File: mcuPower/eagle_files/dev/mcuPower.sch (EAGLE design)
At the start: 8 parts, among them P1 CR2032, P2 CR2032, U1 PQ070XF01SZH

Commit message: various changes + production files. Reroutes, library footprint changes, and moving pot to front side of board
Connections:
- net VOUT: now also R2.E; no longer R2.A
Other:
- moved on the sheet: R2
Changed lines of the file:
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@@
 <instance part="C1" gate="G$1" x="33.02" y="53.34"/>
 <instance part="C2" gate="G$1" x="55.88" y="50.8"/>
-<instance part="R2" gate="1" x="76.2" y="50.8" rot="R180"/>
+<instance part="R2" gate="1" x="76.2" y="50.8"/>
 <instance part="SUPPLY1" gate="G$1" x="53.34" y="96.52"/>
 <instance part="SUPPLY2" gate="GND" x="-10.16" y="27.94"/>
@@
 <wire x1="86.36" y1="58.42" x2="83.82" y2="58.42" width="0.1524" layer="91"/>
 <wire x1="83.82" y1="58.42" x2="83.82" y2="63.5" width="0.1524" layer="91"/>
-<junction x="81.28" y="43.18"/>
-<wire x1="81.28" y1="43.18" x2="68.58" y2="43.18" width="0.1524" layer="91"/>
-<wire x1="68.58" y1="43.18" x2="68.58" y2="50.8" width="0.1524" layer="91"/>
+<pinref part="U1" gate="G$1" pin="VADJ"/>
 <pinref part="R2" gate="1" pin="S"/>
-<wire x1="68.58" y1="50.8" x2="71.12" y2="50.8" width="0.1524" layer="91"/>
-<pinref part="U1" gate="G$1" pin="VADJ"/>
+<wire x1="81.28" y1="48.26" x2="81.28" y2="50.8" width="0.1524" layer="91"/>
+<junction x="81.28" y="48.26"/>
 </segment>
 </net>
@@
 <wire x1="55.88" y1="58.42" x2="55.88" y2="53.34" width="0.1524" layer="91"/>
 <label x="68.58" y="58.42" size="1.778" layer="95"/>
+<pinref part="U1" gate="G$1" pin="VOUT"/>
+<pinref part="R2" gate="1" pin="E"/>
+<wire x1="76.2" y1="55.88" x2="76.2" y2="58.42" width="0.1524" layer="91"/>
 <junction x="76.2" y="58.42"/>
-<pinref part="R2" gate="1" pin="A"/>
-<wire x1="76.2" y1="58.42" x2="76.2" y2="55.88" width="0.1524" layer="91"/>
-<pinref part="U1" gate="G$1" pin="VOUT"/>
 </segment>
 <segment>

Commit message: added extra header pin to stabilize board
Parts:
- added JP2: (no value), adafruit:PINHD-1X1
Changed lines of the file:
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@@
 <part name="P1" library="freddyLibr" deviceset="CR2032" device=""/>
 <part name="P2" library="freddyLibr" deviceset="CR2032" device=""/>
+<part name="JP2" library="adafruit" deviceset="PINHD-1X1" device=""/>
 </parts>
 <sheets>
@@
 <instance part="P1" gate="G$1" x="15.24" y="83.82"/>
 <instance part="P2" gate="G$1" x="27.94" y="88.9"/>
+<instance part="JP2" gate="G$1" x="116.84" y="71.12"/>
 </instances>
 <busses>

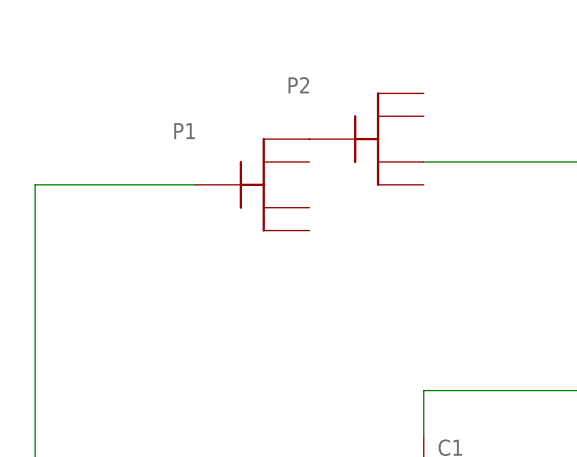
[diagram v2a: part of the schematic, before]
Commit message: new production files for OSHPark. also, copy_eagle version to copy those files to the production file folder. board design itself shows flipped coin battery holder
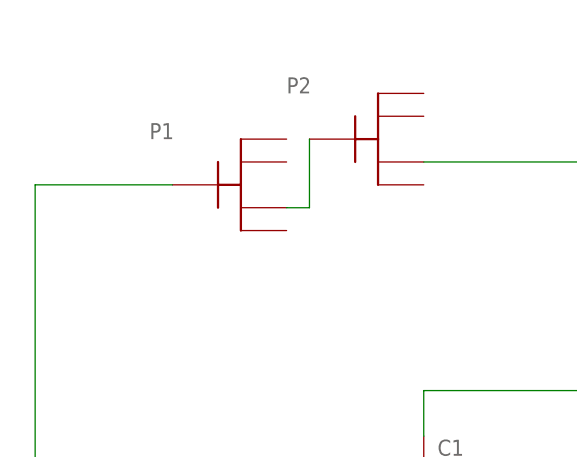
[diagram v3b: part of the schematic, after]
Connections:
- net N$1: now also P1.VCC_3; no longer P1.VCC_1
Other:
- moved on the sheet: P1
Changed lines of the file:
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@@
 <instance part="JP1" gate="G$1" x="114.3" y="50.8" rot="R180"/>
 <instance part="U1" gate="G$1" x="78.74" y="76.2"/>
-<instance part="P1" gate="G$1" x="15.24" y="83.82"/>
+<instance part="P1" gate="G$1" x="12.7" y="83.82"/>
 <instance part="P2" gate="G$1" x="27.94" y="88.9"/>
 <instance part="JP2" gate="G$1" x="116.84" y="71.12"/>
@@
 <wire x1="-10.16" y1="83.82" x2="-10.16" y2="40.64" width="0.1524" layer="91"/>
 <wire x1="-10.16" y1="40.64" x2="-10.16" y2="30.48" width="0.1524" layer="91"/>
-<wire x1="7.62" y1="83.82" x2="-10.16" y2="83.82" width="0.1524" layer="91"/>
+<wire x1="5.08" y1="83.82" x2="-10.16" y2="83.82" width="0.1524" layer="91"/>
 <wire x1="-10.16" y1="40.64" x2="33.02" y2="40.64" width="0.1524" layer="91"/>
 <pinref part="C1" gate="G$1" pin="2"/>
@@
 <net name="N$1" class="0">
 <segment>
-<pinref part="P1" gate="G$1" pin="VCC_1"/>
+<pinref part="P1" gate="G$1" pin="VCC_3"/>
 <pinref part="P2" gate="G$1" pin="GND"/>
+<wire x1="17.78" y1="81.28" x2="20.32" y2="81.28" width="0.1524" layer="91"/>
+<wire x1="20.32" y1="81.28" x2="20.32" y2="88.9" width="0.1524" layer="91"/>
 </segment>
 </net>
